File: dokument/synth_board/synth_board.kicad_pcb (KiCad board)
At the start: 2 copper layers, 99.1 x 99.1 mm, 63 parts, among them IC1 ATMEGA1284-P, U1 74LS165, U10 BUTTON, U11 BUTTON, U12 BUTTON, U13 BUTTON, U14 BUTTON, U15 BUTTON, U16 BUTTON, U17 BUTTON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

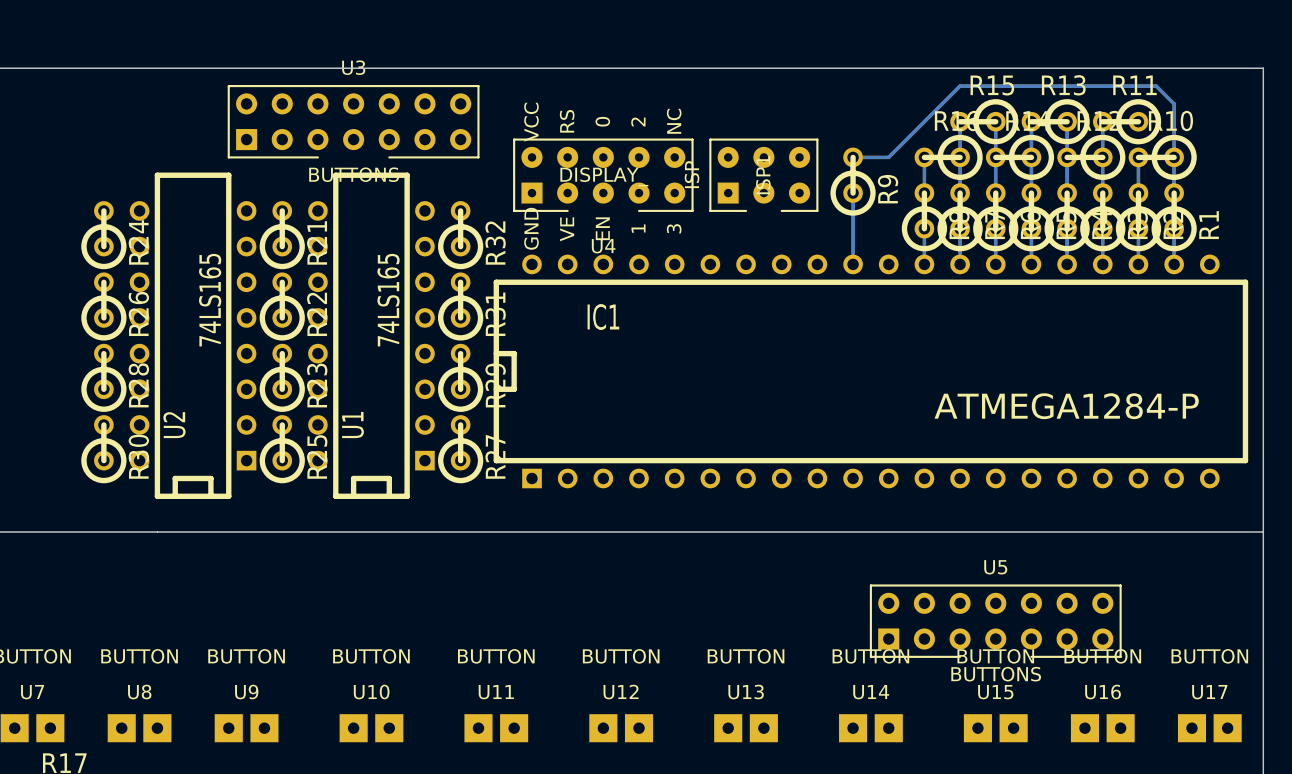
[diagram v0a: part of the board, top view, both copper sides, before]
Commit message: finished routing on main board
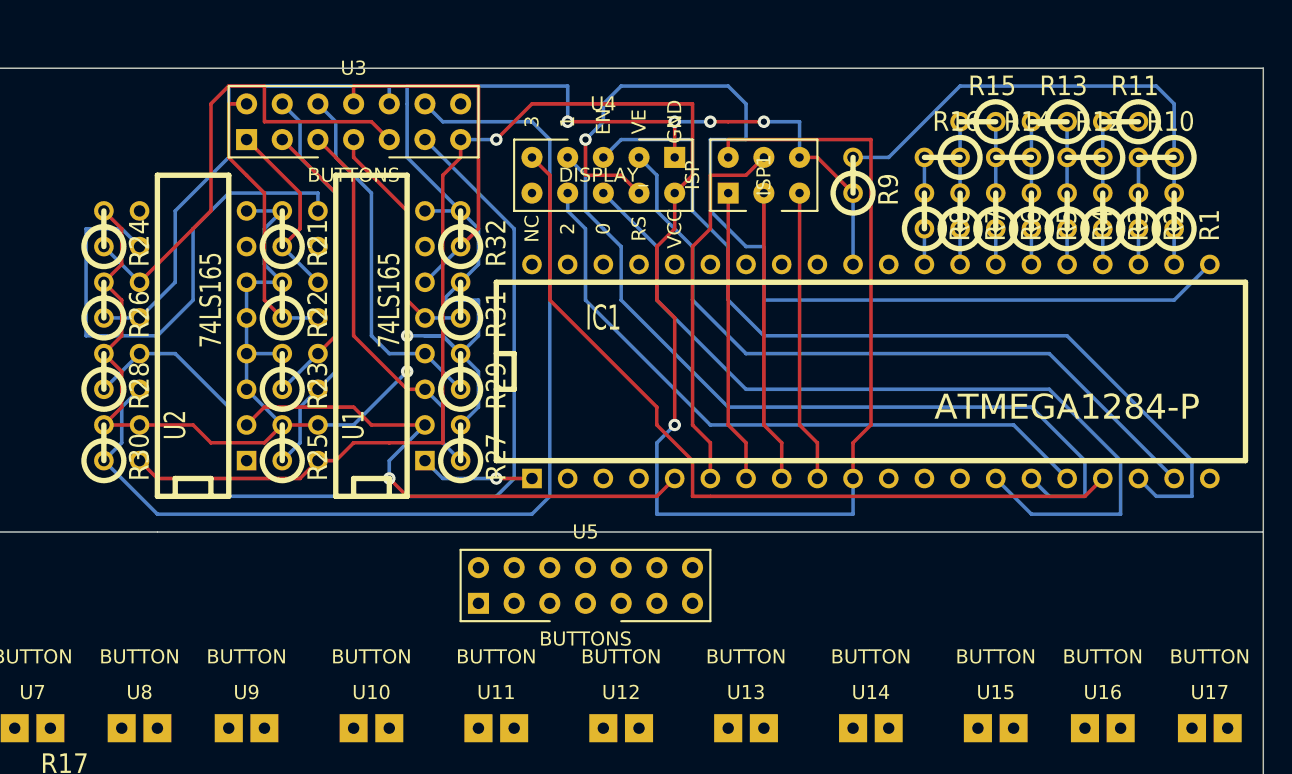
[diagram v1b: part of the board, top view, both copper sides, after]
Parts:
- moved U5 29.3 mm to (67.3, 49.5)
- moved U4 5.08 mm to (72.4, 17.8), turned to 180 degrees
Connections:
- R21 pad 1: N-0000036 -> N-0000037
- R22 pad 1: N-0000037 -> N-0000036
- R23 pad 1: N-0000029 (its old number) -> N-0000035
- R24 pad 1: N-0000035 -> N-0000044
- R25 pad 1: N-0000026 (its old number) -> N-0000039
- R26 pad 1: N-0000032 (its old number) -> N-0000045
- R27 pad 1: N-0000028 (its old number) -> N-0000038
- R28 pad 1: N-0000034 (its old number) -> N-0000046
- R29 pad 1: N-0000027 (its old number) -> N-0000050
- R30 pad 1: N-0000033 (its old number) -> N-0000047
- R31 pad 1: N-0000031 (its old number) -> N-0000048
- R32 pad 1: N-0000030 (its old number) -> N-0000051
- U1 pad 11: N-0000036 -> N-0000037
- U1 pad 12: N-0000037 -> N-0000036
- U1 pad 13: N-0000029 (its old number) -> N-0000035
- U1 pad 14: N-0000026 (its old number) -> N-0000039
- U1 pad 3: N-0000028 (its old number) -> N-0000038
- U1 pad 4: N-0000027 (its old number) -> N-0000050
- U1 pad 5: N-0000031 (its old number) -> N-0000048
- U1 pad 6: N-0000030 (its old number) -> N-0000051
- U2 pad 11: N-0000035 -> N-0000044
- U2 pad 12: N-0000032 (its old number) -> N-0000045
- U2 pad 13: N-0000034 (its old number) -> N-0000046
- U2 pad 14: N-0000033 (its old number) -> N-0000047
- U3 pad 1: (no net) -> N-0000037
- U3 pad 10: (no net) -> N-0000045
- U3 pad 11: (no net) -> N-0000046
- U3 pad 12: (no net) -> N-0000047
- U3 pad 2: (no net) -> N-0000036
- U3 pad 3: (no net) -> N-0000035
- U3 pad 4: (no net) -> N-0000039
- U3 pad 5: (no net) -> N-0000038
- U3 pad 6: (no net) -> N-0000050
- U3 pad 7: (no net) -> N-0000048
- U3 pad 8: (no net) -> N-0000051
- U3 pad 9: (no net) -> N-0000044
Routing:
- net N-0000095: track 5.08 -> 157.0 mm, vias 0 -> 6
- net N-0000034: track 0.00 -> 146.8 mm, vias 0 -> 2
- net N-0000047: track 0.00 -> 75.3 mm
- net N-0000056: track 0.00 -> 72.8 mm, vias 0 -> 1
- net N-0000046: track 0.00 -> 65.5 mm
- net N-0000018: track 0.00 -> 64.0 mm
- net N-0000020: track 0.00 -> 60.7 mm
- net N-0000017: track 0.00 -> 58.6 mm
- net N-0000022: track 0.00 -> 56.4 mm
- net N-0000021: track 0.00 -> 51.3 mm
- net N-0000016: track 0.00 -> 47.7 mm
- net N-0000041: track 0.00 -> 40.0 mm, vias 0 -> 1
- net N-0000053: track 0.00 -> 36.9 mm
- net N-0000044: track 0.00 -> 34.7 mm
- net N-0000045: track 0.00 -> 34.4 mm
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
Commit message: finished with main board, kind of...
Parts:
- added C5: CP1, CP4, F.Cu at (31.8, 94.0)
- added C6: CP1, CP4, F.Cu at (31.8, 91.4)
- added Q1: BC547, TO92, F.Cu at (31.8, 99.1)
- added R33: R, R1, F.Cu at (30.5, 102.9)
- added R34: R, R1, F.Cu at (35.6, 102.9)
- added SP2: SPEAKER, PIN_ARRAY_2X1, F.Cu at (39.4, 92.7)
- added U25: MIC, PIN_ARRAY_2X1, F.Cu at (26.7, 97.8)
- added U26: VCCGND, vccgnd, F.Cu at (38.1, 99.1)
- added U27: SPANNING_SIGNAL, PIN_ARRAY_3X1, F.Cu at (91.4, 15.2)
- added U28: VCCGND, vccgnd, F.Cu at (83.8, 14.6)
- moved SP1 14.5 mm to (41.9, 68.6), turned to 0 degrees
- moved R19 14.0 mm to (47.0, 68.6)
- moved C3 5.68 mm to (41.9, 64.8)
- moved C4 5.24 mm to (41.9, 78.7)
- moved U23 4.58 mm to (34.3, 78.7)
- moved R20 2.84 mm to (43.2, 72.4)
- moved C1 2.54 mm to (43.2, 76.2)
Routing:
- net (no net): track 84.8 -> 15.0 mm
- net N-000007: track 0.00 -> 32.1 mm
- net N-0000027: track 0.00 -> 16.3 mm
- net N-0000032: track 0.00 -> 16.1 mm
- net N-000009: track 0.00 -> 15.0 mm
- net N-000008: track 0.00 -> 13.0 mm
- net N-00000102: track 157.0 -> 169.9 mm
- net N-000005: track 0.00 -> 11.0 mm
- net N-0000082: track 2.54 -> 13.0 mm
- net N-0000070: track 146.8 -> 157.0 mm
- net N-0000099: track 0.00 -> 9.42 mm
- net N-0000031: track 0.00 -> 7.93 mm
- net N-000006: track 0.00 -> 7.40 mm
- net N-0000011: track 0.00 -> 7.40 mm
- net N-000002: track 0.00 -> 4.86 mm
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
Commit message: just going to add pot and electret mic
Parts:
- added 1pin: VAL**, 1pin, F.Cu at (38.1, 15.9)
- added 1pin: VAL**, 1pin, F.Cu at (116.8, 44.5)
- added 1pin: VAL**, 1pin, F.Cu at (115.6, 66.7)
- added 1pin: VAL**, 1pin, F.Cu at (24.1, 66.7)
- added 1pin: VAL**, 1pin, F.Cu at (68.6, 66.7)
- added 1pin: VAL**, 1pin, F.Cu at (47.0, 87.0)
- added 1pin: VAL**, 1pin, F.Cu at (27.9, 71.1)
- added 1pin: VAL**, 1pin, F.Cu at (36.8, 97.2)
- added 1pin: VAL**, 1pin, F.Cu at (22.9, 102.2)
- added C7: C, C1, F.Cu at (88.3, 24.1)
- added U29: 4BUTTON, 4buttons, F.Cu at (116.2, 20.3)
- added X1: CRYSTAL, PIN_ARRAY_2X1, F.Cu at (96.5, 44.5)
- added bigpin: VAL**, bigpin, F.Cu at (115.6, 50.8)
- added bigpin: VAL**, bigpin, F.Cu at (24.1, 50.8)
- added bigpin: VAL**, bigpin, F.Cu at (68.6, 59.1)
- U18, U19, U20, U21: footprint PIN_ARRAY_2X2 -> pcbbutton
- moved U21 96.2 mm to (75.6, 93.3)
- moved U19 94.6 mm to (65.4, 104.1)
- moved U22 81.7 mm to (65.4, 74.3)
- moved U20 72.8 mm to (55.2, 93.3)
- moved U18 71.9 mm to (65.4, 82.5)
- moved R17 8.35 mm to (31.8, 73.0)
- moved C2 8.35 mm to (24.1, 78.1)
- moved C3 8.35 mm to (40.6, 73.0)
- moved C4 8.35 mm to (40.6, 87.0)
- moved U23 8.35 mm to (33.0, 87.0)
- moved C1 8.35 mm to (41.9, 84.5)
- moved R18 8.35 mm to (26.7, 85.7)
- moved R19 8.35 mm to (45.7, 76.8)
- moved R20 8.35 mm to (41.9, 80.6)
- moved U24 8.35 mm to (31.8, 79.4)
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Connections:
- IC1 pad 1: N-0000059 (its old number) -> N-0000061
- IC1 pad 10: N-0000070 (its old number) -> N-0000098
- IC1 pad 12: (no net) -> N-0000042
- IC1 pad 13: (no net) -> N-0000041
- IC1 pad 2: (no net) -> N-0000037
- IC1 pad 20: (no net) -> N-0000040
- IC1 pad 3: (no net) -> N-0000038
- IC1 pad 30: (no net) -> N-0000098
- IC1 pad 32: (no net) -> N-0000086
- IC1 pad 4: (no net) -> N-0000039
- IC1 pad 7: N-0000085 (its old number) -> N-0000079
- ISP1 pad 1: N-0000085 (its old number) -> N-0000079
- ISP1 pad 2: N-0000070 (its old number) -> N-0000098
- U1 pad 1: N-0000059 (its old number) -> N-0000061
- U1 pad 16: N-0000070 (its old number) -> N-0000098
- U2 pad 1: (no net) -> N-0000061
- U2 pad 16: N-0000070 (its old number) -> N-0000098
- U2 pad 9: (no net) -> N-0000079
- U27 pad 1: N-0000070 (its old number) -> N-0000098
- U28 pad 1: N-0000070 (its old number) -> N-0000098
- U3 pad 13: N-0000070 (its old number) -> N-0000098
- U4 pad 2: N-0000070 (its old number) -> N-0000098
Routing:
- net N-0000098: track 0.00 -> 188.9 mm, vias 0 -> 2
- net N-0000070 (its old number): track 157.0 -> 0.00 mm, vias 2 -> 0
- net N-0000056: track 0.00 -> 123.3 mm
- net N-0000079: track 0.00 -> 103.6 mm, vias 0 -> 1
- net N-0000038: track 0.00 -> 94.0 mm, vias 0 -> 2
- net N-0000039: track 0.00 -> 71.6 mm, vias 0 -> 4
- net N-0000037: track 0.00 -> 63.9 mm, vias 0 -> 1
- net N-0000026: track 0.00 -> 46.0 mm
- net N-0000022: track 0.00 -> 45.6 mm
- net N-0000018: track 0.00 -> 40.2 mm
- net N-0000029: track 0.00 -> 37.7 mm
- net N-0000016: track 0.00 -> 36.7 mm
- net N-0000028: track 0.00 -> 34.1 mm
- net N-0000017: track 0.00 -> 27.9 mm
- net N-0000027: track 0.00 -> 23.7 mm
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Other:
- outline, holes or cut-outs redrawn

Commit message: finished yeeeey
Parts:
- added RV1: POT, PIN_ARRAY_3X1, F.Cu at (67.3, 35.6)
- added U30: VCCGND, PIN_ARRAY_2X1, F.Cu at (88.9, 34.3)
- added U31: MIC_INPUT, PIN_ARRAY_1, F.Cu at (85.1, 30.5)
- added bigpin: VAL**, bigpin, F.Cu at (78.7, 72.4)
- added bigpin: VAL**, bigpin, F.Cu at (52.1, 72.4)
- added bigpin: VAL**, bigpin, F.Cu at (52.1, 108.6)
- added bigpin: VAL**, bigpin, F.Cu at (78.7, 108.6)
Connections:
- IC1 pad 33: (no net) -> N-0000036
- IC1 pad 40: (no net) -> N-0000035
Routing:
- net N-0000058: track 0.00 -> 57.4 mm
- net N-0000027: track 0.00 -> 28.9 mm
- net N-0000043: track 0.00 -> 27.3 mm
- net N-0000023: track 0.00 -> 24.1 mm
- net N-0000097: track 188.9 -> 209.3 mm, vias 2 -> 4
- net N-0000035: track 0.00 -> 17.5 mm, vias 0 -> 2
- net N-0000098: track 171.1 -> 183.8 mm
- net N-0000028: track 0.00 -> 9.31 mm
- net N-0000036: track 0.00 -> 3.81 mm
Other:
- outline, holes or cut-outs redrawn

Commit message: added all gerber files incl. .rar
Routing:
- net (no net): track 15.0 -> 0.00 mm
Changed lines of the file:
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@@
     (links 174)
     (no_connects 5)
-    (area 20.269999 12.649999 119.430001 111.810001)
+    (area 19.753223 12.2428 119.946777 111.810001)
     (thickness 1.6)
     (drawings 19)
-    (tracks 635)
+    (tracks 632)
     (zones 0)
     (modules 95)
@@
     (visible_elements FFFFFFBF)
     (pcbplotparams
-      (layerselection 3178497)
+      (layerselection 284196865)
       (usegerberextensions true)
       (excludeedgelayer true)
@@
       (outputformat 1)
       (mirror false)
-      (drillshape 1)
+      (drillshape 0)
       (scaleselection 1)
       (outputdirectory ""))
@@
   (module buttons_conn (layer F.Cu)
     (at 50.8 16.51)
-    (fp_text reference U3 (at 3.81 -3.81) (layer F.SilkS)
+    (fp_text reference U3 (at 3.81 -2.54) (layer F.SilkS)
       (effects (font (size 1 1) (thickness 0.15)))
     )
@@
     (autoplace_cost90 10)
     (autoplace_cost180 10)
-    (fp_text reference R33 (at -1.016 2.54) (layer F.SilkS)
+    (fp_text reference R33 (at -0.635 1.905) (layer F.SilkS)
       (effects (font (size 1.397 1.27) (thickness 0.2032)))
     )
@@
     (descr "Connecteur 3 pins")
     (tags "CONN DEV")
-    (fp_text reference U27 (at 0.254 -2.159) (layer F.SilkS)
+    (fp_text reference U27 (at 0 -1.27) (layer F.SilkS)
       (effects (font (size 1.016 1.016) (thickness 0.1524)))
     )
@@
   (module vccgnd (layer F.Cu)
     (at 83.82 14.605)
-    (fp_text reference U28 (at 0 -2.54) (layer F.SilkS)
+    (fp_text reference U28 (at 0 -0.635) (layer F.SilkS)
       (effects (font (size 1 1) (thickness 0.15)))
     )
@@
   (gr_line (start 34.29 46.99) (end 34.29 12.7) (angle 90) (layer Edge.Cuts) (width 0.1))
   (gr_line (start 119.38 46.99) (end 20.32 46.99) (angle 90) (layer Edge.Cuts) (width 0.1))
-  (segment (start 30.48 -15.24) (end 27.94 -12.7) (width 0.254) (layer F.Cu) (net 0))
-  (segment (start 27.94 -5.08) (end 31.75 -5.08) (width 0.254) (layer F.Cu) (net 0))
-  (segment (start 27.94 -12.7) (end 27.94 -5.08) (width 0.254) (layer F.Cu) (net 0))
   (segment (start 33.02 86.995) (end 34.29 85.725) (width 0.254) (layer F.Cu) (net 1))
   (segment (start 38.1 86.995) (end 39.37 86.995) (width 0.254) (layer F.Cu) (net 1))
